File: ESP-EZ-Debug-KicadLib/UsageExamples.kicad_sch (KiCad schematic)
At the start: 3 parts, among them J1 SOICbite UART, J2 SOICbite JTAG, J3 TC2050 JTAG

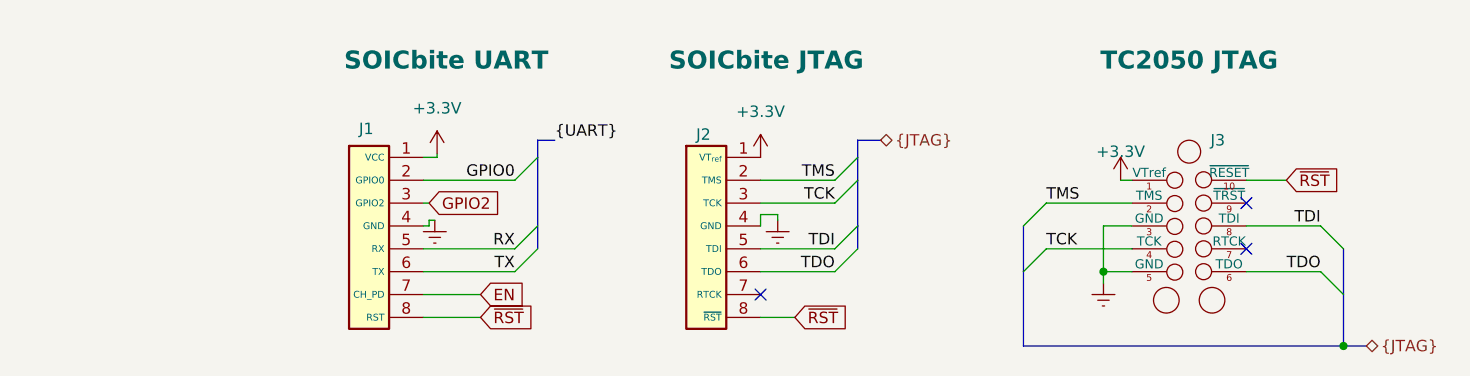
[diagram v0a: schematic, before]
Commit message: Clarification and new example added to SCH, links in library updated
* added link to hackaday article
* added clarification about CH_PD and GPIO2 to SCH
* Added example of ESP32 UART to SCH
* Added pinout table to README
* Updated example schematic
* replaced connector wiring example png with updated version
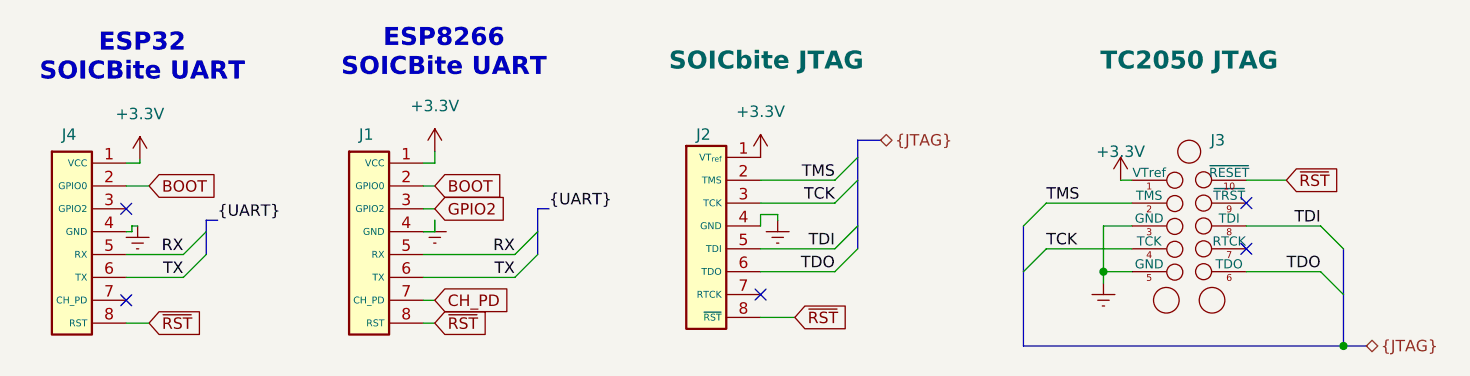
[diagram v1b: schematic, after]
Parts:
- added J4: ESP8266 SOICbite UART, ESP-EZ-Debug:SOIC_clipProgESP, symbol ESP-EZ-Debug:SOICbite-ESP8266
- J1: value SOICbite UART -> ESP8266 SOICbite UART
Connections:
- net +3.3V: now also J4.1 (VCC)
- net Earth: now also J4.4 (GND)
- net RX: now also J4.5 (RX)
- net TX: now also J4.6 (TX)
- net ~{RST}: now also J4.8 (RST)
- net EN renamed CH_PD
- net GPIO0 renamed BOOT
- net BOOT: now also J4.2 (GPIO0)
- no-connect marks 3 -> 5
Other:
- note added: "ESP32 SOICBite UART"
- note added: "ESP8266 SOICBite UART"
- moved on the sheet: J1
